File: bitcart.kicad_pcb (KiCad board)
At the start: 4 copper layers, 110 x 100 mm, 134 parts, among them J1 USB_OTG, J10 Conn_02x03_Odd_Even, J11 10018783-11200TLF, J12 0455580003, J13 Hashboard0, J14 Hashboard1, J15 Hashboard2, J2 690-008-221-904, J3 61900411021, J4 61900411021, J5 61900411021, J6 61900411021, J7 Conn_01x22, J8 Conn_01x02, J9 THD-20-R, Q1 DMP3013SFV-7, U1 FSUSB42MUX, U10 PCA9546ARGVR, U2 USB2514B-I/M2, U3 TPD4EUSB30, U4 AP22653W6, U5 EMC2305-1-AP-TR, U6 74LVC1G07SE-7, U7 MagJack-A70-112-331N126, U8 AP64501SP-13, U9 AP64501SP-13, Y1 24MHz

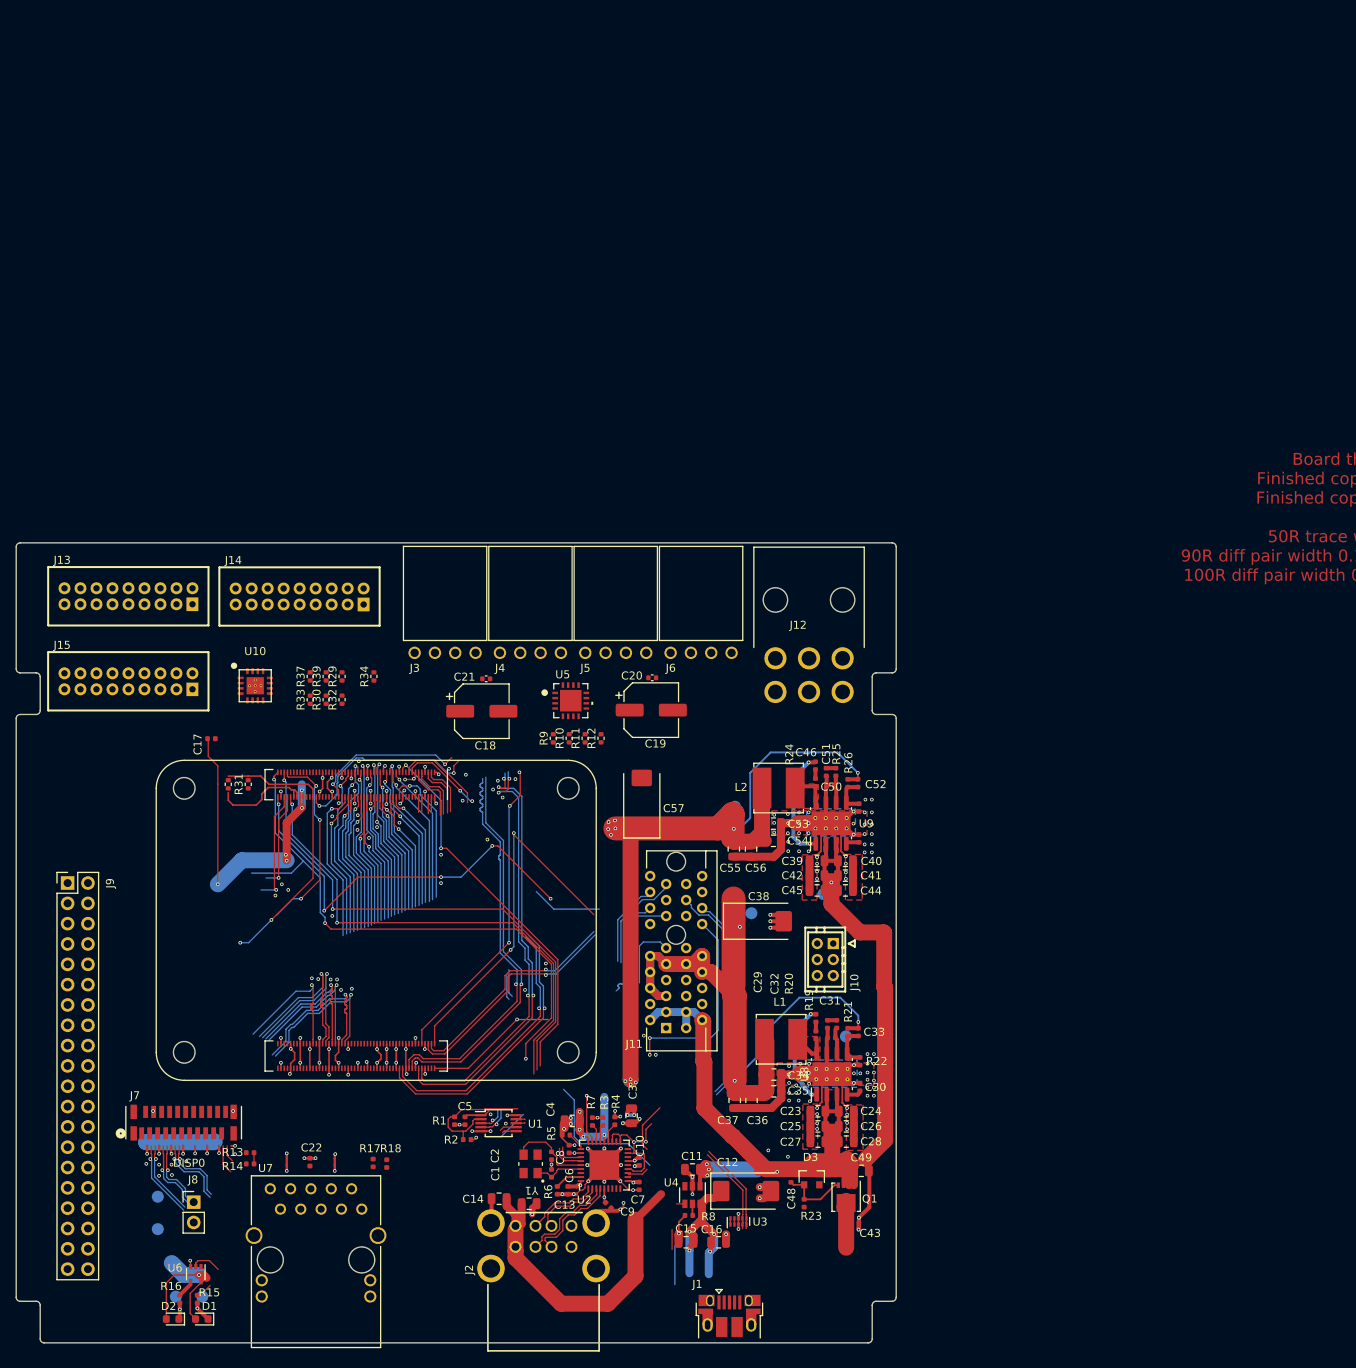
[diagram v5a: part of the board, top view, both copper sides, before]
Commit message: pulled in bitcrane fan and data connectors and edge cuts. most placement done. started routing
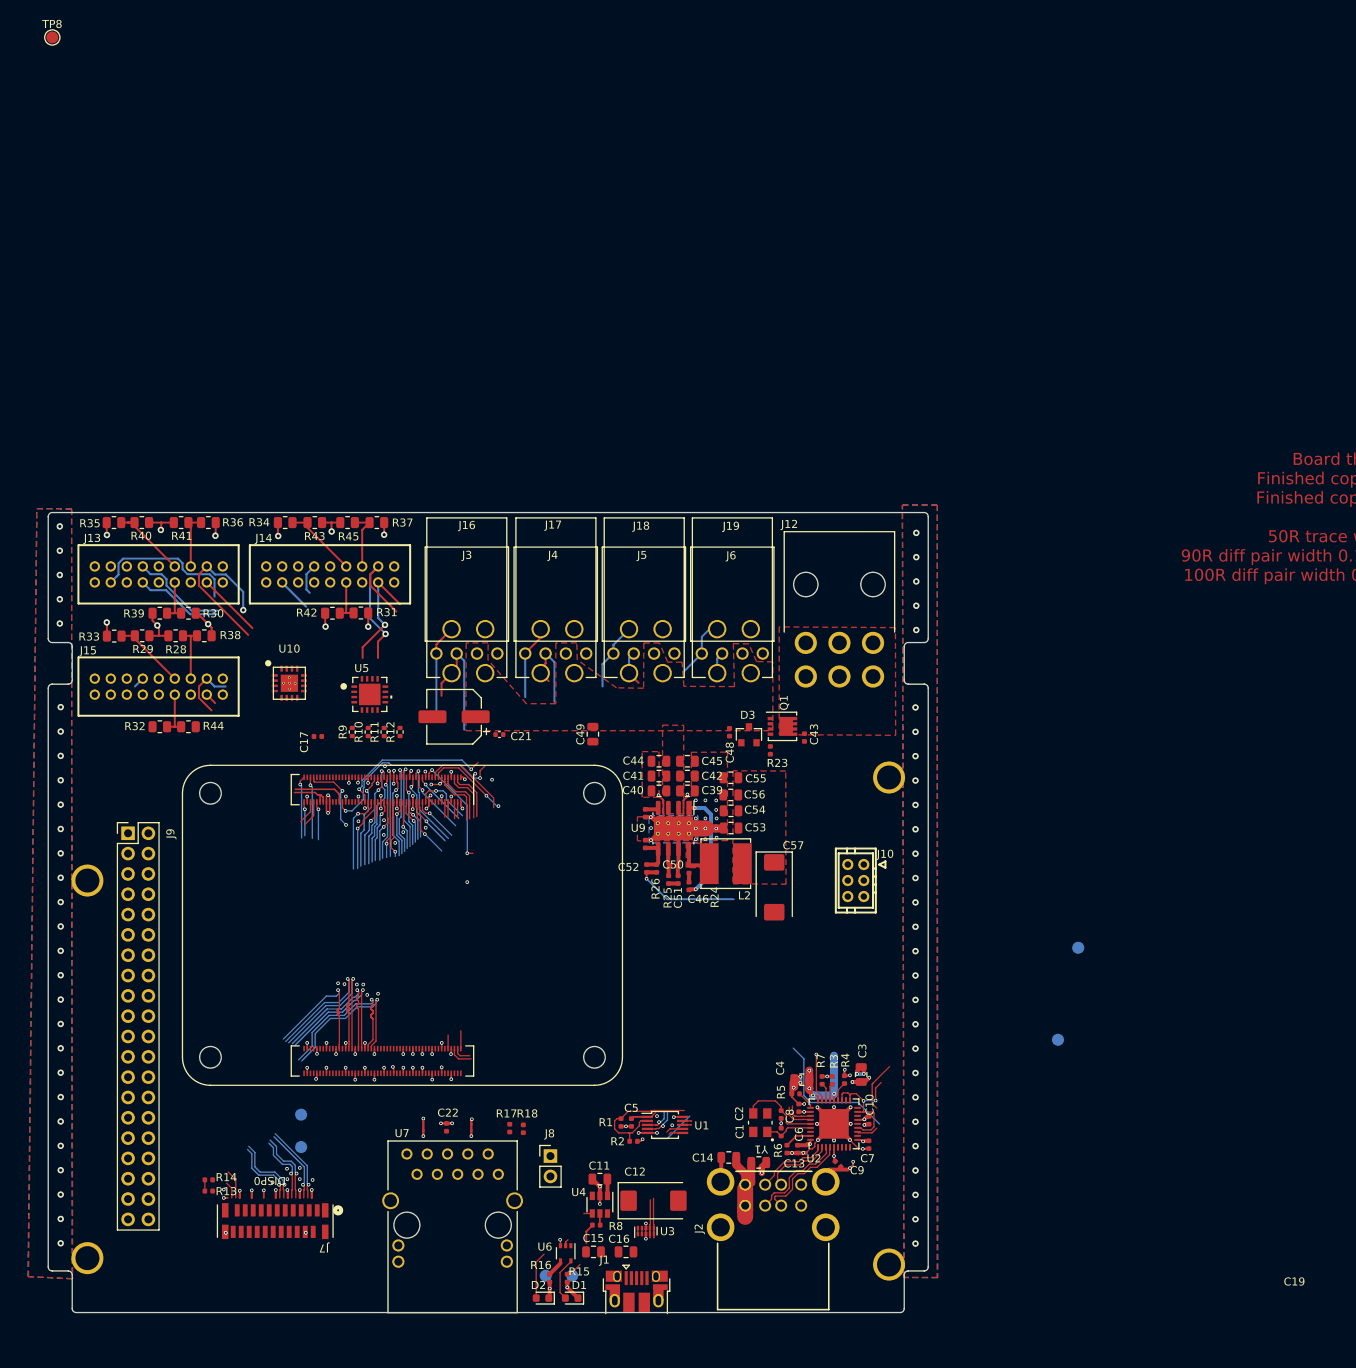
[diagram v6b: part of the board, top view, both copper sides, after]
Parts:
- removed C18: 220uF, Capacitor_SMD:CP_Elec_6.3x7.7
- removed C20, C29, C30: 0.1uF, Capacitor_SMD:C_0402_1005Metric
- removed C23, C24, C25, C26, C27, C28: 10u 35v, Capacitor_SMD:C_0805_2012Metric
- removed C31, C33: nf, Capacitor_SMD:C_0402_1005Metric
- removed C32: 1.2nF, Capacitor_SMD:C_0402_1005Metric
- removed C34, C35, C36, C37: 10u, Capacitor_SMD:C_0805_2012Metric
- removed C38: 100uF, Capacitor_Tantalum_SMD:CP_EIA-7343-31_Kemet-D
- removed J11: 10018783-11200TLF, CM4IO:PCIex1-36
- removed L1: SRN6045TA-3R3Y, Inductor_SMD:L_Bourns_SRN6045TA
- removed R19: 10R, Resistor_SMD:R_0402_1005Metric
- removed R20: 12K 1%, Resistor_SMD:R_0402_1005Metric
- removed R21: 47K 1%, Resistor_SMD:R_0402_1005Metric
- removed R22: 15K 1%, Resistor_SMD:R_0402_1005Metric
- removed TP5: TestPoint, TestPoint:TestPoint_Pad_D1.5mm
- removed U8: AP64501SP-13, Package_SO:SOIC-8-1EP_3.9x4.9mm_P1.27mm_EP2.95x4.9mm_Mask2.71x3.4mm_ThermalVias
- added H1: MountingHole_Pad, bitcrane:MountingHole_3mm_Pad, F.Cu at (182.8, 71.5)
- added H2: MountingHole_Pad, bitcrane:MountingHole_3mm_Pad, F.Cu at (182.8, 132.4)
- added H3: MountingHole_Pad, bitcrane:MountingHole_3mm_Pad, F.Cu at (82.6, 84.4)
- added H4: MountingHole_Pad, bitcrane:MountingHole_3mm_Pad, F.Cu at (82.6, 131.6)
- added J16: 0353180420, bitcrane:MOLEX_353180420, F.Cu at (128.1, 53.0)
- added J17: 0353180420, bitcrane:MOLEX_353180420, F.Cu at (139.2, 53.0)
- added J18: 0353180420, bitcrane:MOLEX_353180420, F.Cu at (150.3, 53.0)
- added J19: 0353180420, bitcrane:MOLEX_353180420, F.Cu at (161.3, 53.0)
- added R35: 4.7K, Resistor_SMD:R_0805_2012Metric, F.Cu at (85.9, 39.7)
- added R36: 4.7K, Resistor_SMD:R_0805_2012Metric, F.Cu at (97.7, 39.7)
- added R38: 4.7K, Resistor_SMD:R_0805_2012Metric, F.Cu at (97.2, 53.8)
- added R40: 4.7K, Resistor_SMD:R_0805_2012Metric, F.Cu at (89.4, 39.7)
- added R41: 4.7K, Resistor_SMD:R_0805_2012Metric, F.Cu at (94.3, 39.7)
- added R42: 4.7K, Resistor_SMD:R_0805_2012Metric, F.Cu at (113.2, 51.0)
- added R43: 4.7K, Resistor_SMD:R_0805_2012Metric, F.Cu at (111.0, 39.7)
- added R44: 4.7K, Resistor_SMD:R_0805_2012Metric, F.Cu at (95.2, 65.2)
- added R45: 4.7K, Resistor_SMD:R_0805_2012Metric, F.Cu at (115.1, 39.7)
- C39, C40, C41, C42, C44, C45: value 10u 35v -> 10uF 35v
- C53, C54, C55, C56: value 10u -> 10uF
- R24: value 10R -> 10
- R25: value 20K 1% -> 20k
- R26: value 12K 1% -> 12k
- R27: value 2.2K 1% -> 2.2k
- R28, R29, R30, R31, R32, R33, R34, R37, R39: footprint Resistor_SMD:R_0402_1005Metric -> Resistor_SMD:R_0805_2012Metric
- TP8: moved to F.Cu
- moved TP8 159.5 mm to (78.2, -21.0)
- moved C49 64.1 mm to (145.8, 66.1), turned to -90 degrees
- moved C43 61.1 mm to (172.2, 66.5), turned to -90 degrees
- moved Q1 59.4 mm to (169.5, 65.1), turned to 0 degrees
- moved R23 56.8 mm to (168.0, 68.1)
- moved C48 56.3 mm to (162.8, 65.9)
- moved D3 55.8 mm to (165.3, 66.2)
- moved TP7 49.8 mm to (203.9, 104.3)
- moved TP3 46.3 mm to (143.2, 133.8)
- moved D1 46.3 mm to (143.1, 136.6)
- moved D2 46.3 mm to (139.5, 136.6)
- moved R16 46.3 mm to (140.4, 134.1)
- moved TP4 46.3 mm to (139.9, 133.8)
- moved U6 46.3 mm to (142.4, 131.0)
- moved R15 46.3 mm to (142.6, 134.1)
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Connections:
- J4 pad 1: unconnected-(J4-Pin_1-Pad1) -> GND
- J5 pad 1: unconnected-(J5-Pin_1-Pad1) -> GND
- Module1 pad 102: /CM4_HighSpeed/PCIE_CLK_nREQ -> unconnected-(Module1B-PCIe_CLK_nREQ-Pad102)
- Module1 pad 109: /CM4_HighSpeed/PCIE_nRST -> unconnected-(Module1B-PCIe_nRST-Pad109)
- Module1 pad 110: /CM4_HighSpeed/PCIE_CLK_P -> unconnected-(Module1B-PCIe_CLK_P-Pad110)
- Module1 pad 112: /CM4_HighSpeed/PCIE_CLK_N -> unconnected-(Module1B-PCIe_CLK_N-Pad112)
- Module1 pad 116: /CM4_HighSpeed/PCIE_RX_P -> unconnected-(Module1B-PCIe_RX_P-Pad116)
- Module1 pad 118: /CM4_HighSpeed/PCIE_RX_N -> unconnected-(Module1B-PCIe_RX_N-Pad118)
- Module1 pad 122: /CM4_HighSpeed/PCIE_TX_P -> unconnected-(Module1B-PCIe_TX_P-Pad122)
- Module1 pad 124: /CM4_HighSpeed/PCIE_TX_N -> unconnected-(Module1B-PCIe_TX_N-Pad124)
- R13 pad 1: /CM4_GPIO ( Ethernet, GPIO, SDCARD)/+3.3v -> /+3.3v
- R14 pad 1: /CM4_GPIO ( Ethernet, GPIO, SDCARD)/+3.3v -> /+3.3v
- R28 pad 1: GND -> /hashboards/A0-1
- R28 pad 2: /hashboards/A1-0 -> GND
- R29 pad 1: GND -> /hashboards/A2-1
- R29 pad 2: /hashboards/A1-2 -> GND
- R30 pad 1: /hashboards/A0-2 -> /hashboards/3V3
- R30 pad 2: /hashboards/3V3 -> /hashboards/A1-0
- R31 pad 1: /hashboards/A0-0 -> /hashboards/3V3
- R31 pad 2: GND -> /hashboards/A1-2
- R32 pad 1: /hashboards/A2-2 -> /hashboards/3V3
- R32 pad 2: GND -> /hashboards/A1-1
- R33 pad 1: /hashboards/A2-0 -> /hashboards/3V3
- R33 pad 2: GND -> /hashboards/A0-1
- R34 pad 2: /hashboards/A1-1 -> /hashboards/A0-2
- R37 pad 1: /hashboards/A0-1 -> /hashboards/3V3
- R37 pad 2: GND -> /hashboards/A2-2
- R39 pad 1: /hashboards/A2-1 -> GND
- R39 pad 2: GND -> /hashboards/A1-0
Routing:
- net /+12v: track 132.5 -> 0.00 mm, vias 1 -> 0
- net /PCIe-connector/+3.3v: track 95.9 -> 0.00 mm, vias 3 -> 0
- net /+5v: track 105.0 -> 16.1 mm, vias 14 -> 1
- net /+3.3v: track 136.4 -> 51.4 mm, vias 21 -> 14
- net GND: track 255.9 -> 172.9 mm, vias 234 -> 208
- net /CM4_HighSpeed/PCIE_CLK_N: track 67.2 -> 0.00 mm, vias 3 -> 0
- net /CM4_HighSpeed/PCIE_CLK_P: track 64.9 -> 0.00 mm, vias 3 -> 0
- net /CM4_GPIO ( Ethernet, GPIO, SDCARD)/GLOBAL_EN: track 72.4 -> 7.85 mm, vias 3 -> 1
- net /CM4_HighSpeed/PCIE_RX_N: track 60.8 -> 0.00 mm, vias 1 -> 0
- net /CM4_HighSpeed/PCIE_RX_P: track 60.5 -> 0.00 mm, vias 1 -> 0
- net /CM4_GPIO ( Ethernet, GPIO, SDCARD)/nPWR_LED: track 68.5 -> 8.59 mm, vias 2 -> 1
- net /USB2-HUB/VBUS: track 69.2 -> 11.5 mm, vias 4 -> 0
- net /CM4_GPIO ( Ethernet, GPIO, SDCARD)/RUN_PG: track 61.8 -> 4.52 mm, vias 2 -> 1
- net /CM4_HighSpeed/PCIE_CLK_nREQ: track 56.5 -> 0.00 mm, vias 3 -> 0
- net /CM4_HighSpeed/PCIE_TX_P: track 54.9 -> 0.00 mm, vias 1 -> 0
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- added copper zone on F.Cu, net /+5v
- added copper zone on In1.Cu, net GND
- added copper zone on F.Cu, net Net-(Q1-D)
- removed copper zone on F.Cu, net Net-(U8-SW)
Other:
- outline, holes or cut-outs redrawn

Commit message: more placement
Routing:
- net GND: track 172.9 -> 174.7 mm, vias 208 -> 206
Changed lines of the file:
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@@
   (segment (start 124.47 108.5) (end 124.47 107.8) (width 0.2) (layer "F.Cu") (net 1))
   (segment (start 117.27 105.4) (end 117.27 104.71001) (width 0.2) (layer "F.Cu") (net 1))
+  (segment (start 157.688553 73.792422) (end 157.926053 73.792422) (width 0.23) (layer "F.Cu") (net 1))
   (segment (start 116.07 105.42) (end 116.07 106.1) (width 0.2) (layer "F.Cu") (net 1))
   (segment (start 113.09 39.66) (end 114.1975 39.66) (width 0.25) (layer "F.Cu") (net 1))
-  (segment (start 153.938553 73.592422) (end 153.938553 73.742422) (width 0.23) (layer "F.Cu") (net 1))
   (segment (start 122.07 107.81001) (end 122.08001 107.8) (width 0.2) (layer "F.Cu") (net 1))
   (segment (start 157.088553 74.392422) (end 157.088553 76.642422) (width 0.23) (layer "F.Cu") (net 1))
@@
   (segment (start 171.054 109.294) (end 171.485 109.725) (width 0.5) (layer "F.Cu") (net 1))
   (segment (start 175.914 114.818) (end 175.914 112.729) (width 0.5) (layer "F.Cu") (net 1))
+  (segment (start 153.651053 73.742422) (end 153.101053 73.192422) (width 0.23) (layer "F.Cu") (net 1))
   (segment (start 125.27 74.58) (end 125.27 75.1) (width 0.2) (layer "F.Cu") (net 1))
   (segment (start 116.47 72.11137) (end 116.406823 72.174547) (width 0.2) (layer "F.Cu") (net 1))
@@
   (segment (start 120.87 108.5) (end 120.87 108.35) (width 0.2) (layer "F.Cu") (net 1))
   (segment (start 119.27 74.58) (end 119.27 75.4) (width 0.2) (layer "F.Cu") (net 1))
-  (segment (start 157.688553 73.592422) (end 157.688553 73.792422) (width 0.23) (layer "F.Cu") (net 1))
   (segment (start 125.27 74.58) (end 125.27 73.980058) (width 0.2) (layer "F.Cu") (net 1))
   (segment (start 179.635 108.575) (end 179.635 108.0375) (width 0.5) (layer "F.Cu") (net 1))
@@
   (segment (start 175.914 114.818) (end 177.91 116.814) (width 0.5) (layer "F.Cu") (net 1))
   (segment (start 178.31 119.95) (end 177.91 120.35) (width 0.2) (layer "F.Cu") (net 1))
+  (segment (start 157.926053 73.792422) (end 158.526053 73.192422) (width 0.23) (layer "F.Cu") (net 1))
   (segment (start 170.9505 109.294) (end 170.9505 110.214474) (width 1) (layer "F.Cu") (net 1))
   (segment (start 178.31 119.55) (end 178.31 119.95) (width 0.2) (layer "F.Cu") (net 1))
@@
   (segment (start 124.45999 105.41001) (end 124.45999 106.1) (width 0.2) (layer "F.Cu") (net 1))
   (segment (start 114.87 108.5) (end 114.87 107.8) (width 0.2) (layer "F.Cu") (net 1))
+  (segment (start 153.938553 73.742422) (end 153.651053 73.742422) (width 0.23) (layer "F.Cu") (net 1))
   (segment (start 120.87 107.8) (end 120.77 107.7) (width 0.13) (layer "F.Cu") (net 1))
   (segment (start 128.07 74.58) (end 128.07 73.9) (width 0.2) (layer "F.Cu") (net 1))
@@
   (via (at 126.88001 104.699345) (size 0.45) (drill 0.25) (layers "F.Cu" "B.Cu") (net 1))
   (via (at 186.2 43.985) (size 0.8) (drill 0.4) (layers "F.Cu" "B.Cu") (free) (net 1))
-  (via (at 157.588553 73.642422) (size 0.45) (drill 0.25) (layers "F.Cu" "B.Cu") (net 1))
   (via (at 110.635 123.08) (size 0.45) (drill 0.25) (layers "F.Cu" "B.Cu") (net 1))
   (via (at 177.91 120.35) (size 0.45) (drill 0.25) (layers "F.Cu" "B.Cu") (net 1))
@@
   (via (at 99.885 128.43) (size 0.45) (drill 0.25) (layers "F.Cu" "B.Cu") (net 1))
   (via (at 186.2 53.09) (size 0.8) (drill 0.4) (layers "F.Cu" "B.Cu") (free) (net 1))
-  (via (at 153.988553 73.742422) (size 0.45) (drill 0.25) (layers "F.Cu" "B.Cu") (net 1))
   (via (at 125.69 109.29) (size 0.45) (drill 0.25) (layers "F.Cu" "B.Cu") (net 1))
   (via (at 129.47 75.4) (size 0.45) (drill 0.25) (layers "F.Cu" "B.Cu") (net 1))
@@
     (polygon
       (pts
-        (xy 154.478553 64.982422)
-        (xy 157.118553 65.002422)
-        (xy 157.128553 76.072422)
-        (xy 154.488553 76.052422)
+        (xy 154.008553 64.902422)
+        (xy 157.528553 64.952422)
+        (xy 157.538553 76.022422)
+        (xy 154.018553 75.972422)
       )
     )
@@
     (polygon
       (pts
-        (xy 151.938553 68.292422)
-        (xy 154.038553 68.292422)
-        (xy 154.038553 73.992422)
-        (xy 151.938553 73.992422)
+        (xy 151.51 68.322422)
+        (xy 153.61 68.322422)
+        (xy 153.61 74.022422)
+        (xy 151.51 74.022422)
       )
     )

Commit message: lots of routing. lots more to do
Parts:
- added R19: 10k, Resistor_SMD:R_0402_1005Metric, F.Cu at (123.4, 23.0)
- added R20: 10k, Resistor_SMD:R_0402_1005Metric, F.Cu at (123.4, 25.0)
- added R21: 10k, Resistor_SMD:R_0402_1005Metric, F.Cu at (123.4, 27.0)
- added R22: 10k, Resistor_SMD:R_0402_1005Metric, F.Cu at (123.4, 29.0)
- R1, R13, R14, R2: value 2.2K 1% -> 2.2k 1%
- R10, R11, R12, R9: value 36K -> 36k
- R17, R18: value 470R -> 470
- R23, R6: value 12K 1% -> 12k 1%
- R3, R4, R5, R7: value 36K 1% -> 36k 1%
- R8: value 15K 1% -> 15k 1%
- moved TP2 21.7 mm to (112.7, 135.1)
- moved C12 21.5 mm to (165.4, 106.6), turned to 90 degrees
- moved U4 20.9 mm to (160.6, 109.3)
- moved C11 20.9 mm to (160.6, 106.2)
- moved R8 20.5 mm to (159.8, 112.1)
- moved TP1 17.9 mm to (114.9, 134.7)
- moved C22 11.2 mm to (116.3, 116.5)
- moved R14 3.92 mm to (94.0, 123.0), turned to 180 degrees
- moved R13 3.06 mm to (100.8, 122.9)
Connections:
- net /+12v renamed /12V
- net /+3.3v renamed /3V3
- net /+5v renamed /5V
- net /CM4_HighSpeed/+3.3v renamed /CM4_HighSpeed/3V3
- J13 pad 11: /CM4_GPIO ( Ethernet, GPIO, SDCARD)/GPIO14 -> /CM4_GPIO ( Ethernet, GPIO, SDCARD)/GPIO8
- J13 pad 12: /CM4_GPIO ( Ethernet, GPIO, SDCARD)/GPIO15 -> /CM4_GPIO ( Ethernet, GPIO, SDCARD)/GPIO9
- J13 pad 15: /CM4_GPIO ( Ethernet, GPIO, SDCARD)/GPIO17 -> /CM4_GPIO ( Ethernet, GPIO, SDCARD)/GPIO11
- J13 pad 5: /CM4_GPIO ( Ethernet, GPIO, SDCARD)/GPIO16 -> /CM4_GPIO ( Ethernet, GPIO, SDCARD)/GPIO10
- J15 pad 11: /CM4_GPIO ( Ethernet, GPIO, SDCARD)/GPIO8 -> /CM4_GPIO ( Ethernet, GPIO, SDCARD)/GPIO14
- J15 pad 12: /CM4_GPIO ( Ethernet, GPIO, SDCARD)/GPIO12 -> /CM4_GPIO ( Ethernet, GPIO, SDCARD)/GPIO15
- J15 pad 15: /CM4_GPIO ( Ethernet, GPIO, SDCARD)/GPIO11 -> /CM4_GPIO ( Ethernet, GPIO, SDCARD)/GPIO17
- J15 pad 5: /CM4_GPIO ( Ethernet, GPIO, SDCARD)/GPIO10 -> /CM4_GPIO ( Ethernet, GPIO, SDCARD)/GPIO16
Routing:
- net /CM4_GPIO ( Ethernet, GPIO, SDCARD)/GPIO11: track 6.04 -> 112.4 mm, vias 1 -> 4
- net /CM4_GPIO ( Ethernet, GPIO, SDCARD)/GPIO9: track 6.95 -> 107.6 mm, vias 1 -> 3
- net /CM4_GPIO ( Ethernet, GPIO, SDCARD)/GPIO16: track 11.4 -> 106.4 mm, vias 1 -> 2
- net /CM4_GPIO ( Ethernet, GPIO, SDCARD)/GPIO8: track 11.5 -> 104.3 mm, vias 1 -> 2
- net /CM4_GPIO ( Ethernet, GPIO, SDCARD)/GPIO6: track 7.45 -> 99.9 mm
- net /CM4_GPIO ( Ethernet, GPIO, SDCARD)/GPIO5: track 9.11 -> 99.4 mm
- net /CM4_GPIO ( Ethernet, GPIO, SDCARD)/ID_SD: track 7.64 -> 84.8 mm
- net /CM4_GPIO ( Ethernet, GPIO, SDCARD)/GPIO4: track 8.48 -> 84.4 mm
- net /CM4_GPIO ( Ethernet, GPIO, SDCARD)/GPIO7: track 15.5 -> 91.2 mm
- net /CM4_GPIO ( Ethernet, GPIO, SDCARD)/ID_SC: track 12.3 -> 87.4 mm
- net /CM4_GPIO ( Ethernet, GPIO, SDCARD)/GPIO26: track 7.46 -> 79.5 mm
- net /CM4_GPIO ( Ethernet, GPIO, SDCARD)/GPIO21: track 7.01 -> 77.8 mm
- net /CM4_GPIO ( Ethernet, GPIO, SDCARD)/GPIO19: track 5.97 -> 73.2 mm
- net /CM4_GPIO ( Ethernet, GPIO, SDCARD)/GPIO20: track 7.93 -> 74.5 mm
- net /CM4_GPIO ( Ethernet, GPIO, SDCARD)/GPIO13: track 6.22 -> 67.9 mm
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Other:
- board text added: "HB2 - P4"
